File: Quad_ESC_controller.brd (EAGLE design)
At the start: 25.4 x 38.1 mm, 36 parts, among them IC1 OP-AMP, Y1 ECS-80-S-4X

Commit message: check this
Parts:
- removed J1, J10, J11, J2, J3, J6, J8: (no value), SparkFun-Connectors:1X01
- removed OP-AMP, OP-AMP1: LM2904S, IC, LM2904:SO08
- J7: device SparkFun-Connectors:1X01 -> SparkFun-Connectors:1X06
- moved RESET 27.2 mm to (9.32, 29.3), turned to 270 degrees
- moved C10 26.3 mm to (14.9, 3.05), turned to 270 degrees
- moved SV2 19.6 mm to (23.1, 31.5), turned to 180 degrees
- moved C7 19.4 mm to (8.89, 24.1)
- moved R7 17.9 mm to (17.1, 11.0), turned to 270 degrees
- moved U$8 17.7 mm to (17.4, 2.67), flipped to the top
- moved D1 16.6 mm to (17.1, 14.6), turned to 270 degrees
- moved J7 14.9 mm to (1.35, 14.1), turned to 270 degrees
- moved R2 14.4 mm to (6.48, 22.0), flipped to the top
- moved C1 13.9 mm to (13.8, 16.1), flipped to the bottom, turned to 270 degrees
- moved U$2 13.5 mm to (5.21, 23.4), turned to 90 degrees
- moved C2 11.8 mm to (9.78, 12.1), flipped to the bottom
- moved IC1 9.91 mm to (11.6, 4.06), turned to 90 degrees
- moved C5 9.64 mm to (9.40, 16.1), flipped to the bottom, turned to 270 degrees
- moved C8 9.58 mm to (21.7, 26.7), flipped to the bottom, turned to 270 degrees
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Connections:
- net +3V3: no longer OP-AMP.8, OP-AMP1.8
- net ADC: now also J7.1
- net CAN_H: no longer J10.1
- net CAN_L: no longer J11.1
- net CAN_RX: no longer J7.1
- net CAN_TX: no longer J6.1
- net GND: no longer OP-AMP.4, OP-AMP1.4
- net N$6: now also IC1.2; no longer J8.1, OP-AMP1.2
- net NRST: no longer J3.1
- net SWCLK: no longer J1.1
- net SWDIO: no longer J2.1
- net TIM3_CH1: now also J7.3
- net TIM3_CH2: now also J7.4
- net TIM3_CH3: now also J7.5
- net TIM3_CH4: now also J7.6
- net TLM: now also IC1.1; no longer OP-AMP1.1
- net TLM_ESC: now also IC1.3, J7.2; no longer OP-AMP1.3
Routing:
- net TIM3_CH4: track 7.86 -> 38.5 mm
- net CAN_L: track 43.8 -> 17.5 mm, vias 2 -> 1
- net TIM3_CH3: track 7.78 -> 33.6 mm, vias 0 -> 1
- net NRST: track 75.6 -> 50.9 mm, vias 5 -> 0
- net TIM3_CH2: track 7.69 -> 29.6 mm, vias 0 -> 1
- net CAN_H: track 38.4 -> 17.1 mm, vias 0 -> 1
- net TLM: track 30.0 -> 9.50 mm, vias 3 -> 1
- net TIM3_CH1: track 7.61 -> 27.6 mm, vias 0 -> 2
- net TLM_ESC: track 16.0 -> 34.2 mm, vias 1 -> 3
- net +3V3: track 103.6 -> 87.9 mm, vias 6 -> 5
- net SWDIO: track 28.7 -> 42.8 mm, vias 2 -> 1
- net SWCLK: track 29.5 -> 42.8 mm
- net ADC: track 7.45 -> 19.2 mm, vias 0 -> 1
- net CAN_RX: track 25.4 -> 15.0 mm, vias 4 -> 2
- net N$6: track 15.0 -> 6.72 mm
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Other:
- board size 25.4 x 38.1 mm -> 25.8 x 34.2 mm
- board text added: "C:/Users/Rach s PC/Desktop/kingsman logo.bmp'"

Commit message: added silkscreen, removed caps
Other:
- board text added: "X14 ESC Controller Peter Sperry Erin Park, Read Hedl Katherine Sandys 1/7/2022"
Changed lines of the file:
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@@
 <?xml version="1.0" encoding="utf-8"?>
 <!DOCTYPE eagle SYSTEM "eagle.dtd">
-<eagle version="9.6.2">
+<eagle version="9.5.0">
 <drawing>
 <settings>
@@
 <wire x1="0" y1="34.163" x2="0" y2="0" width="0" layer="20"/>
 <text x="2.921" y="0.0635" size="0.0254" layer="200" font="vector">C:/Users/Rach s PC/Desktop/kingsman logo.bmp'</text>
+<text x="3.937" y="15.621" size="0.4572" layer="25" rot="R90">X14 ESC Controller
+Peter Sperry
+Erin Park, Read Hedl
+Katherine Sandys
+1/7/2022</text>
 </plain>
 <attributes>
@@
 </polygon>
 <contactref element="U$3" pad="10"/>
-<via x="1.143" y="17.399" extent="1-16" drill="0.35"/>
-<via x="1.3589" y="21.2852" extent="1-16" drill="0.35"/>
+<via x="1.651" y="19.812" extent="1-16" drill="0.35"/>
+<via x="0.9779" y="22.0472" extent="1-16" drill="0.35"/>
 <via x="9.779" y="20.193" extent="1-16" drill="0.35"/>
 <via x="6.35" y="23.622" extent="1-16" drill="0.35"/>
@@
 </drawing>
 <compatibility>
+<note version="6.3" minversion="6.2.2" severity="warning">
+Since Version 6.2.2 text objects can contain more than one line,
+which will not be processed correctly with this version.
+</note>
 <note version="8.2" severity="warning">
 Since Version 8.2, EAGLE supports online libraries. The ids

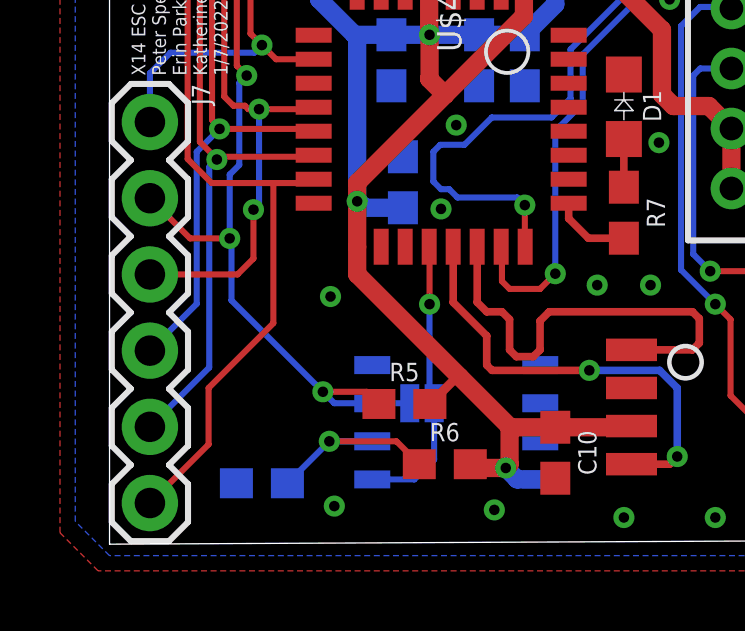
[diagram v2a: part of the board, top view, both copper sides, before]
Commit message: fixed jumper under da chip
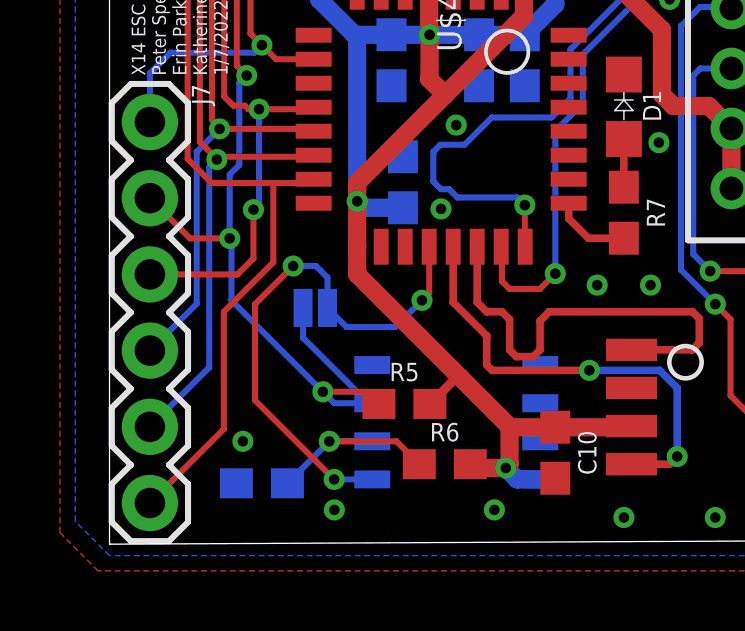
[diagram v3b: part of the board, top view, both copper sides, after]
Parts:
- moved JP1 4.77 mm to (6.86, 7.87)
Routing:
- net TLM: track 9.50 -> 18.0 mm, vias 1 -> 3
- net TLM_ESC: track 34.2 -> 37.2 mm
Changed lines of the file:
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@@
 <?xml version="1.0" encoding="utf-8"?>
 <!DOCTYPE eagle SYSTEM "eagle.dtd">
-<eagle version="9.5.0">
+<eagle version="9.6.2">
 <drawing>
 <settings>
@@
 <attribute name="VALUE" x="5.08" y="2.794" size="0.6096" layer="28" font="vector" ratio="20" rot="MR180" align="top-center"/>
 </element>
-<element name="JP1" library="SparkFun-Jumpers" library_urn="urn:adsk.eagle:library:528" package="SMT-JUMPER_2_NO_SILK" package3d_urn="urn:adsk.eagle:package:39279/1" value="JUMPER-SMT_2_NO_SILK" x="10.414" y="4.699" smashed="yes" rot="MR180">
-<attribute name="NAME" x="10.414" y="3.556" size="0.6096" layer="26" font="vector" ratio="20" rot="MR180" align="bottom-center"/>
+<element name="JP1" library="SparkFun-Jumpers" library_urn="urn:adsk.eagle:library:528" package="SMT-JUMPER_2_NO_SILK" package3d_urn="urn:adsk.eagle:package:39279/1" value="JUMPER-SMT_2_NO_SILK" x="6.858" y="7.874" smashed="yes" rot="MR180">
+<attribute name="NAME" x="6.858" y="6.731" size="0.6096" layer="26" font="vector" ratio="20" rot="MR180" align="bottom-center"/>
 </element>
 <element name="J7" library="SparkFun-Connectors" library_urn="urn:adsk.eagle:library:513" package="1X06" package3d_urn="urn:adsk.eagle:package:38009/1" value="" x="1.3462" y="14.0716" smashed="yes" rot="R270">
@@
 <via x="20.193" y="0.889" extent="1-16" drill="0.35"/>
 <via x="17.145" y="0.889" extent="1-16" drill="0.35"/>
-<via x="7.493" y="1.27" extent="1-16" drill="0.35"/>
+<via x="7.493" y="1.143" extent="1-16" drill="0.35"/>
 <via x="12.827" y="1.143" extent="1-16" drill="0.35"/>
 <contactref element="IC1" pad="4"/>
 <contactref element="R8" pad="1"/>
-<via x="7.366" y="8.255" extent="1-16" drill="0.35"/>
+<via x="4.445" y="3.429" extent="1-16" drill="0.35"/>
 </signal>
 <signal name="+3V3">
@@
 <contactref element="J7" pad="6"/>
 <wire x1="2.6042" y1="12.839" x2="3.4052" y2="12.038" width="0.2032" layer="1"/>
-<wire x1="1.3462" y1="1.3716" x2="3.302" y2="3.3274" width="0.2032" layer="1"/>
-<wire x1="3.302" y1="3.3274" x2="3.302" y2="5.207" width="0.2032" layer="1"/>
-<wire x1="5.461" y1="7.366" x2="5.461" y2="12.038" width="0.2032" layer="1"/>
-<wire x1="3.302" y1="5.207" x2="5.461" y2="7.366" width="0.2032" layer="1"/>
+<wire x1="1.3462" y1="1.3716" x2="3.81" y2="3.8354" width="0.2032" layer="1"/>
+<wire x1="3.81" y1="3.8354" x2="3.81" y2="7.747" width="0.2032" layer="1"/>
+<wire x1="5.461" y1="9.398" x2="5.461" y2="12.038" width="0.2032" layer="1"/>
+<wire x1="3.81" y1="7.747" x2="5.461" y2="9.398" width="0.2032" layer="1"/>
 </signal>
 <signal name="CAN_H">
@@
 <signal name="TLM">
 <contactref element="U$4" pad="PA10"/>
-<wire x1="10.655" y1="9.915" x2="10.668" y2="9.902" width="0.2032" layer="1"/>
-<wire x1="10.668" y1="9.902" x2="10.668" y2="8.001" width="0.2032" layer="1"/>
 <contactref element="IC1" pad="1"/>
 <contactref element="JP1" pad="2"/>
-<wire x1="8.757" y1="2.159" x2="10.16" y2="2.159" width="0.2032" layer="16"/>
-<via x="10.668" y="8.001" extent="1-16" drill="0.35"/>
-<wire x1="10.8204" y1="2.8194" x2="10.8204" y2="4.699" width="0.2032" layer="16"/>
-<wire x1="10.16" y1="2.159" x2="10.8204" y2="2.8194" width="0.2032" layer="16"/>
-<wire x1="10.8204" y1="4.699" x2="10.668" y2="4.8514" width="0.2032" layer="16"/>
-<wire x1="10.668" y1="4.8514" x2="10.668" y2="8.001" width="0.2032" layer="16"/>
+<via x="10.414" y="8.128" extent="1-16" drill="0.35"/>
+<wire x1="8.757" y1="2.159" x2="7.487" y2="2.159" width="0.2032" layer="16"/>
+<wire x1="7.487" y1="2.159" x2="4.8514" y2="4.7946" width="0.2032" layer="1"/>
+<wire x1="7.2644" y1="7.874" x2="7.2644" y2="8.89" width="0.2032" layer="16"/>
+<wire x1="7.2644" y1="8.89" x2="6.8834" y2="9.271" width="0.2032" layer="16"/>
+<wire x1="6.8834" y1="9.271" x2="6.1214" y2="9.271" width="0.2032" layer="16"/>
+<wire x1="6.1214" y1="9.271" x2="4.8514" y2="8.001" width="0.2032" layer="1"/>
+<wire x1="4.8514" y1="8.001" x2="4.8514" y2="4.7946" width="0.2032" layer="1"/>
+<via x="7.487" y="2.159" extent="1-16" drill="0.35"/>
+<via x="6.1214" y="9.271" extent="1-16" drill="0.35"/>
+<wire x1="7.2644" y1="7.874" x2="7.8994" y2="7.239" width="0.2032" layer="16"/>
+<wire x1="9.525" y1="7.239" x2="7.8994" y2="7.239" width="0.2032" layer="16"/>
+<wire x1="9.525" y1="7.239" x2="10.414" y2="8.128" width="0.2032" layer="16"/>
+<wire x1="10.655" y1="9.915" x2="10.655" y2="8.369" width="0.2032" layer="1"/>
+<wire x1="10.655" y1="8.369" x2="10.414" y2="8.128" width="0.2032" layer="1"/>
 </signal>
 <signal name="ADC">
@@
 <wire x1="7.112" y1="5.08" x2="8.5734" y2="5.08" width="0.2032" layer="1"/>
 <wire x1="8.5734" y1="5.08" x2="8.9798" y2="4.6736" width="0.2032" layer="1"/>
-<wire x1="10.0076" y1="4.699" x2="8.757" y2="4.699" width="0.2032" layer="16"/>
+<wire x1="6.4516" y1="7.874" x2="6.4516" y2="6.8774" width="0.2032" layer="16"/>
+<wire x1="8.63" y1="4.699" x2="6.4516" y2="6.8774" width="0.2032" layer="16"/>
+<wire x1="8.63" y1="4.699" x2="8.757" y2="4.699" width="0.2032" layer="16"/>
 <contactref element="J7" pad="2"/>
 <wire x1="4.2418" y1="27.4482" x2="4.2418" y2="15.9512" width="0.2032" layer="1"/>

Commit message: made it nice
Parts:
- moved JP1 1.02 mm to (6.35, 8.76), turned to 0 degrees
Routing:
- net TLM: track 18.0 -> 15.5 mm
- net TLM_ESC: track 37.2 -> 38.4 mm
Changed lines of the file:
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@@
 <attribute name="VALUE" x="5.08" y="2.794" size="0.6096" layer="28" font="vector" ratio="20" rot="MR180" align="top-center"/>
 </element>
-<element name="JP1" library="SparkFun-Jumpers" library_urn="urn:adsk.eagle:library:528" package="SMT-JUMPER_2_NO_SILK" package3d_urn="urn:adsk.eagle:package:39279/1" value="JUMPER-SMT_2_NO_SILK" x="6.858" y="7.874" smashed="yes" rot="MR180">
-<attribute name="NAME" x="6.858" y="6.731" size="0.6096" layer="26" font="vector" ratio="20" rot="MR180" align="bottom-center"/>
+<element name="JP1" library="SparkFun-Jumpers" library_urn="urn:adsk.eagle:library:528" package="SMT-JUMPER_2_NO_SILK" package3d_urn="urn:adsk.eagle:package:39279/1" value="JUMPER-SMT_2_NO_SILK" x="6.35" y="8.763" smashed="yes" rot="MR0">
+<attribute name="NAME" x="6.35" y="9.906" size="0.6096" layer="26" font="vector" ratio="20" rot="MR0" align="bottom-center"/>
 </element>
 <element name="J7" library="SparkFun-Connectors" library_urn="urn:adsk.eagle:library:513" package="1X06" package3d_urn="urn:adsk.eagle:package:38009/1" value="" x="1.3462" y="14.0716" smashed="yes" rot="R270">
@@
 <via x="10.414" y="8.128" extent="1-16" drill="0.35"/>
 <wire x1="8.757" y1="2.159" x2="7.487" y2="2.159" width="0.2032" layer="16"/>
-<wire x1="7.487" y1="2.159" x2="4.8514" y2="4.7946" width="0.2032" layer="1"/>
-<wire x1="7.2644" y1="7.874" x2="7.2644" y2="8.89" width="0.2032" layer="16"/>
-<wire x1="7.2644" y1="8.89" x2="6.8834" y2="9.271" width="0.2032" layer="16"/>
-<wire x1="6.8834" y1="9.271" x2="6.1214" y2="9.271" width="0.2032" layer="16"/>
-<wire x1="6.1214" y1="9.271" x2="4.8514" y2="8.001" width="0.2032" layer="1"/>
-<wire x1="4.8514" y1="8.001" x2="4.8514" y2="4.7946" width="0.2032" layer="1"/>
 <via x="7.487" y="2.159" extent="1-16" drill="0.35"/>
-<via x="6.1214" y="9.271" extent="1-16" drill="0.35"/>
-<wire x1="7.2644" y1="7.874" x2="7.8994" y2="7.239" width="0.2032" layer="16"/>
-<wire x1="9.525" y1="7.239" x2="7.8994" y2="7.239" width="0.2032" layer="16"/>
-<wire x1="9.525" y1="7.239" x2="10.414" y2="8.128" width="0.2032" layer="16"/>
+<wire x1="9.16449375" y1="6.87849375" x2="6.37049375" y2="6.87849375" width="0.2032" layer="16"/>
+<wire x1="9.16449375" y1="6.87849375" x2="10.414" y2="8.128" width="0.2032" layer="16"/>
 <wire x1="10.655" y1="9.915" x2="10.655" y2="8.369" width="0.2032" layer="1"/>
 <wire x1="10.655" y1="8.369" x2="10.414" y2="8.128" width="0.2032" layer="1"/>
+<wire x1="7.487" y1="2.159" x2="5.6924" y2="3.9536" width="0.2032" layer="1"/>
+<via x="6.37049375" y="6.87849375" extent="1-16" drill="0.35"/>
+<wire x1="5.6924" y1="3.9536" x2="5.6924" y2="6.2004" width="0.2032" layer="1"/>
+<wire x1="5.6924" y1="6.2004" x2="6.37049375" y2="6.87849375" width="0.2032" layer="1"/>
+<wire x1="6.37049375" y1="6.87849375" x2="5.9436" y2="7.3053875" width="0.2032" layer="16"/>
+<wire x1="5.9436" y1="7.3053875" x2="5.9436" y2="8.763" width="0.2032" layer="16"/>
 </signal>
 <signal name="ADC">
@@
 <contactref element="R5" pad="1"/>
 <contactref element="JP1" pad="1"/>
-<via x="7.112" y="5.08" extent="1-16" drill="0.35"/>
-<wire x1="7.112" y1="5.08" x2="7.493" y2="4.699" width="0.2032" layer="16"/>
-<wire x1="7.493" y1="4.699" x2="8.757" y2="4.699" width="0.2032" layer="16"/>
-<wire x1="7.112" y1="5.08" x2="8.5734" y2="5.08" width="0.2032" layer="1"/>
-<wire x1="8.5734" y1="5.08" x2="8.9798" y2="4.6736" width="0.2032" layer="1"/>
-<wire x1="6.4516" y1="7.874" x2="6.4516" y2="6.8774" width="0.2032" layer="16"/>
-<wire x1="8.63" y1="4.699" x2="6.4516" y2="6.8774" width="0.2032" layer="16"/>
+<via x="6.604" y="5.715" extent="1-16" drill="0.35"/>
+<wire x1="6.604" y1="5.715" x2="6.604" y2="5.207" width="0.2032" layer="16"/>
+<wire x1="7.112" y1="4.699" x2="6.604" y2="5.207" width="0.2032" layer="16"/>
+<wire x1="7.112" y1="4.699" x2="8.757" y2="4.699" width="0.2032" layer="16"/>
+<wire x1="6.604" y1="5.715" x2="6.985" y2="6.096" width="0.2032" layer="1"/>
+<wire x1="8.0654" y1="6.096" x2="6.985" y2="6.096" width="0.2032" layer="1"/>
+<wire x1="8.9798" y1="5.1816" x2="8.0654" y2="6.096" width="0.2032" layer="1"/>
+<wire x1="8.9798" y1="5.1816" x2="8.9798" y2="4.6736" width="0.2032" layer="1"/>
 <wire x1="8.63" y1="4.699" x2="8.757" y2="4.699" width="0.2032" layer="16"/>
 <contactref element="J7" pad="2"/>
@@
 <wire x1="4.2418" y1="15.9512" x2="4.572" y2="15.621" width="0.2032" layer="1"/>
 <via x="4.572" y="15.621" extent="1-16" drill="0.35"/>
-<wire x1="4.00540625" y1="10.19319375" x2="4.064" y2="10.1346" width="0.2032" layer="16"/>
-<wire x1="4.064" y1="10.1346" x2="4.064" y2="8.128" width="0.2032" layer="16"/>
-<wire x1="7.112" y1="5.08" x2="4.064" y2="8.128" width="0.2032" layer="16"/>
+<wire x1="4.00540625" y1="10.19319375" x2="4.0132" y2="10.1854" width="0.2032" layer="16"/>
+<wire x1="4.0132" y1="10.1854" x2="4.0132" y2="8.3058" width="0.2032" layer="16"/>
+<wire x1="6.604" y1="5.715" x2="4.0132" y2="8.3058" width="0.2032" layer="16"/>
 <wire x1="1.3462" y1="11.5316" x2="2.68460625" y2="10.19319375" width="0.2032" layer="1"/>
 <wire x1="2.68460625" y1="10.19319375" x2="4.00540625" y2="10.19319375" width="0.2032" layer="1"/>
@@
 <wire x1="4.3258" y1="12.640625" x2="4.3258" y2="15.3748" width="0.2032" layer="16"/>
 <wire x1="4.3258" y1="15.3748" x2="4.572" y2="15.621" width="0.2032" layer="16"/>
+<wire x1="6.7564" y1="8.763" x2="6.5659" y2="8.9535" width="0.2032" layer="16"/>
+<wire x1="6.5659" y1="8.9535" x2="6.5659" y2="9.52425" width="0.2032" layer="16"/>
+<wire x1="6.5659" y1="9.52425" x2="5.89695625" y2="10.19319375" width="0.2032" layer="16"/>
+<wire x1="5.89695625" y1="10.19319375" x2="4.00540625" y2="10.19319375" width="0.2032" layer="16"/>
 </signal>
 <signal name="N$6">
